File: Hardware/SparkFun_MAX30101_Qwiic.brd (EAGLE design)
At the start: 25.4 x 25.4 mm, 64 parts, among them J1 PTH, J3 QWIIC_RA, J5 QWIIC_RA, Q6 20V/0.2A/8MHz/1.2Ω/1Vth, Q8 20V/0.2A/8MHz/1.2Ω/1Vth, U1 1.8V/100mA, U3 MAX30101EFD

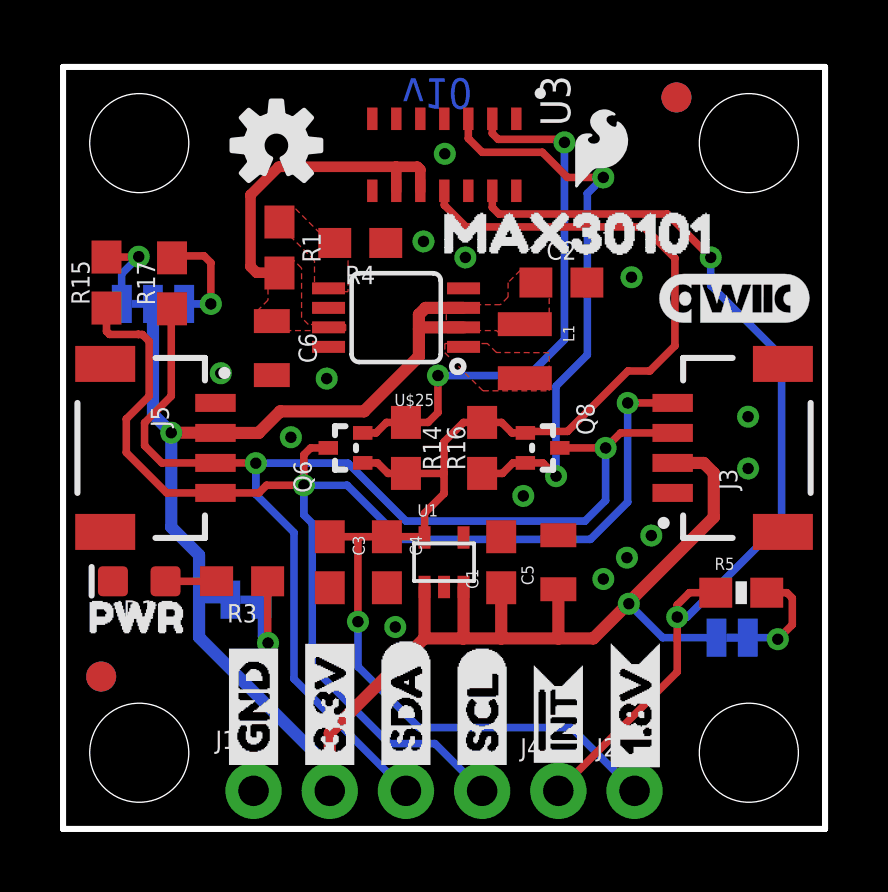
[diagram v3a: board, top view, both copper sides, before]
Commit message: design review #2 changes (post DC-DC converter addition)
-cleaned up sch around DC-DC converter
-added silk outline to MAX30101 IC
-replaced 4.7K resistor to updated package (without silk under it)
-updated Mosfets on logic level translation to latest library devices
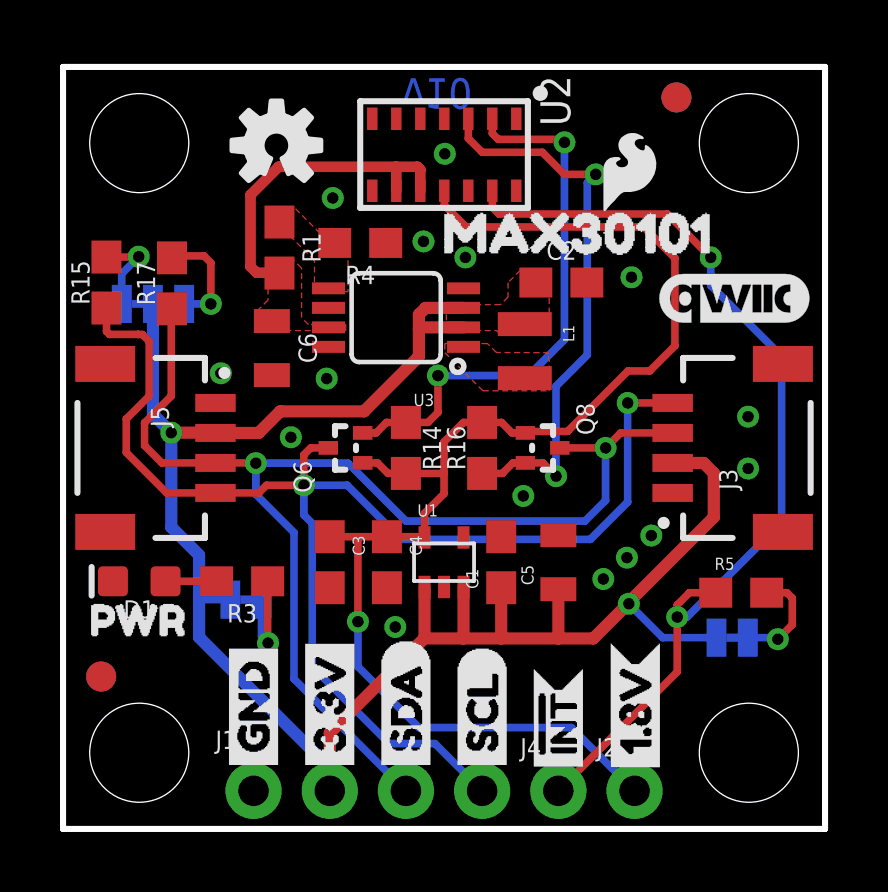
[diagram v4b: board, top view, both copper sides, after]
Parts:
- removed U$25: PAM2401, SparkFun-IC-Power:MSOP8
- added U2: MAX30101EFD, SparkFun-IC-Special-Function:14_PIN_OESIP
- R14, R15, R16, R17, R3: device SparkFun-Resistors:0603@1 -> SparkFun-Resistors:0603
- R5: value 4.7K -> 4.7k; device SparkFun-Resistors:0603-RES -> SparkFun-Resistors:0603
- U3: value MAX30101EFD -> PAM2401; device SparkFun-IC-Special-Function:14_PIN_OESIP -> SparkFun-IC-Power:MSOP8
- moved U3 5.67 mm to (11.1, 17.0), turned to 90 degrees
- moved LOGO4 1.23 mm to (18.9, 21.9)
- moved U$11 0.13 mm to (16.5, 1.40)
- moved U$3 0.13 mm to (16.5, 1.40)
- moved U$26 0.11 mm to (-0.03, 6.96)
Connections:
- net !INT: now also U2.P13; no longer U3.P13
- net 1.8V: now also U2.P11; no longer U3.P11
- net 3.3V: now also U3.2, U3.3; no longer U$25.2, U$25.3
- net 5V: now also U2.P10, U2.P9, U3.7; no longer U$25.7, U3.P10, U3.P9
- net GND: now also U2.P12, U2.P4, U3.4, U3.8; no longer U$25.4, U$25.8, U3.P12, U3.P4
- net LV_SCL: now also U2.P2; no longer U3.P2
- net LV_SDA: now also U2.P3; no longer U3.P3
- net N$2: now also U3.5; no longer U$25.5
- net N$3: now also U3.1; no longer U$25.1

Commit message: Added more bypass caps to 5V and 1.8V, bumped version to v11
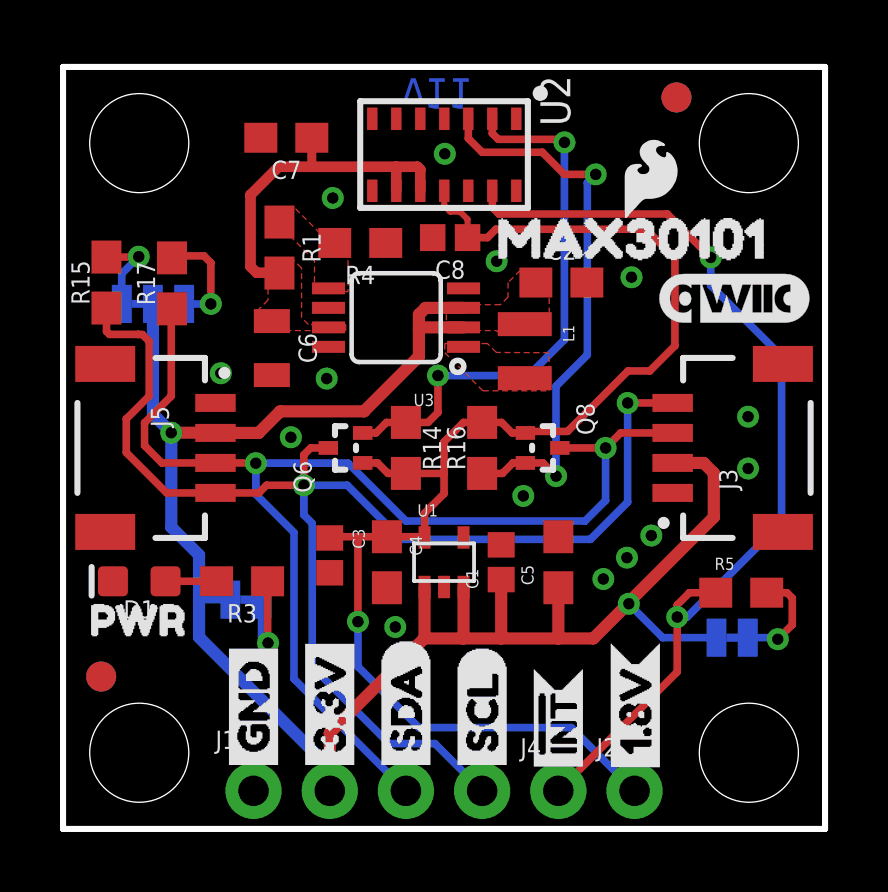
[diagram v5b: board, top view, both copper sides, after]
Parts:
- added C7: 10uF, SparkFun-Capacitors:0603
- added C8: 0.1uF, SparkFun-Capacitors:0402
- C1, C3: device SparkFun-Capacitors:0603 -> SparkFun-Capacitors:0402
- C4: value 4.7uF -> 10uF
- C5: device SparkFun-Capacitors:0805 -> SparkFun-Capacitors:0603
- moved LOGO2 17.4 mm to (22.1, 13.9), flipped to the bottom
- moved U$4 1.81 mm to (13.3, 19.7)
- moved LOGO4 0.75 mm to (19.6, 21.7)
- moved C3 0.23 mm to (8.89, 9.12)
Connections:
- net 1.8V: now also C8.1
- net 5V: now also C7.1
- net GND: now also C7.2, C8.2
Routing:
- net 5V: track 11.0 -> 12.0 mm
- net 1.8V: track 45.9 -> 46.5 mm
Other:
- board text added: "v11"
- board text removed: "v10"

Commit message: Updated name silk to "Photodetector"
Also bumped version to v12 on sch and brd
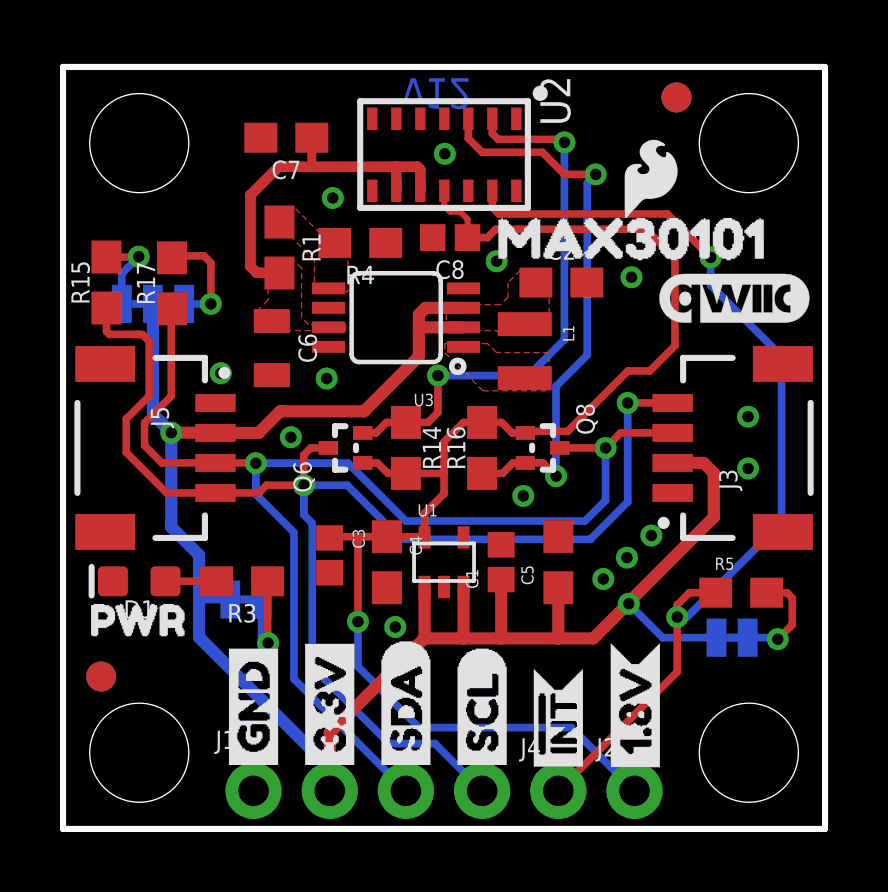
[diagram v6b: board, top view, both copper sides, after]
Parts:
- removed U$17: (no value), buzzard_labels (7):PARTICLE1
- removed U$18: (no value), buzzard_labels (7):SENSOR2
- added U$1: (no value), buzzard_labels:PHOTODETECTOR3
- moved U$24 0.25 mm to (18.5, 16.3)
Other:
- board text added: "v12"
- board text removed: "v11"
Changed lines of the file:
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@@
 <layer number="27" name="tValues" color="7" fill="1" visible="no" active="yes"/>
 <layer number="28" name="bValues" color="7" fill="1" visible="no" active="yes"/>
-<layer number="29" name="tStop" color="5" fill="5" visible="yes" active="yes"/>
+<layer number="29" name="tStop" color="5" fill="5" visible="no" active="yes"/>
 <layer number="30" name="bStop" color="7" fill="6" visible="no" active="yes"/>
 <layer number="31" name="tCream" color="7" fill="4" visible="no" active="yes"/>
@@
 <wire x1="0" y1="25.4" x2="25.4" y2="25.4" width="0.2032" layer="20"/>
 <wire x1="25.4" y1="0" x2="0" y2="0" width="0.2032" layer="20"/>
-<text x="11.303" y="25.019" size="1.016" layer="16" font="vector" ratio="20" rot="SMR180">v11</text>
+<text x="11.303" y="25.019" size="1.016" layer="16" font="vector" ratio="20" rot="SMR180">v12</text>
 <text x="27.94" y="-16.51" size="1.778" layer="51" font="vector" ratio="10">Pete Lewis</text>
 <text x="8.89" y="-19.05" size="1.778" layer="51" font="vector" ratio="10">Based on a design for the MAX30105 by N. Seidle</text>
@@
 </element>
 <element name="U$16" library="SparkFun-Aesthetics" package="QWIIC_5.5MM" value="" x="13.0048" y="13.9954" smashed="yes" rot="MR0"/>
-<element name="U$17" library="buzzard_labels (7)" package="PARTICLE1" value="" x="20.6248" y="18.2118" smashed="yes" rot="MR0"/>
-<element name="U$18" library="buzzard_labels (7)" package="SENSOR2" value="" x="13.335" y="18.1864" smashed="yes" rot="MR0"/>
-<element name="U$24" library="buzzard_labels (7)" package="MAX301010" value="" x="18.4658" y="16.002" smashed="yes" rot="MR0"/>
+<element name="U$24" library="buzzard_labels (7)" package="MAX301010" value="" x="18.4658" y="16.256" smashed="yes" rot="MR0"/>
 <element name="LOGO3" library="SparkFun-Aesthetics" package="QWIIC_5MM" value="QWIIC_LOGO_5MM" x="22.352" y="17.7038" smashed="yes"/>
 <element name="U$15" library="buzzard_labels (9)" package="ADR#_0X570" value="" x="17.2212" y="12.1412" smashed="yes" rot="MR0"/>
@@
 <attribute name="VALUE" x="12.9032" y="20.4724" size="0.6096" layer="27" font="vector" ratio="20" rot="R180" align="top-center"/>
 </element>
+<element name="U$1" library="buzzard_labels" package="PHOTODETECTOR3" value="" x="20.5994" y="18.1864" smashed="yes" rot="MR0"/>
 </elements>
 <signals>
